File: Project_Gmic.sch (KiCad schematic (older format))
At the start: 44 parts, among them J1 SecondaryBoard_L, J2 SecondaryBoard_R, SW1 SW_SPST, U1 ADA4807-1, U2 ADA4807-4, U3 ADA4807-1, U4 XC6351A120MR-G

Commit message: butterworth filter, new aop, cleaning
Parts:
- removed C2, C5: 100pF, Capacitor_SMD:C_0805_2012Metric, symbol Device:C
- removed R11, R12, R6: 10k, Resistor_SMD:R_0805_2012Metric, symbol Device:R
- removed R4, R7: 80k, Resistor_SMD:R_0805_2012Metric, symbol Device:R
- removed SW1: SW_SPST, Button_Switch_SMD:SW_DIP_SPSTx01_Slide_9.78x4.72mm_W8.61mm_P2.54mm, symbol Switch:SW_SPST
- removed U1, U3: ADA4807-1, Package_TO_SOT_SMD:SOT-23-6_Handsoldering, symbol Amplifier_Operational:ADA4807-1
- removed U2: ADA4807-4, Package_SO:SOIC-14_3.9x8.7mm_P1.27mm, symbol Amplifier_Operational:ADA4807-4
- added C? (x3): 100pF, Capacitor_SMD:C_0805_2012Metric, symbol Device:C
- added J?: AudioJack2_Ground, symbol Connector:AudioJack2_Ground
- added J?: USB_C_Receptacle_USB2.0, symbol Connector:USB_C_Receptacle_USB2.0
- added R? (x3): 80k, Resistor_SMD:R_0805_2012Metric, symbol Device:R
- added RV?: R_Potentiometer, symbol Device:R_Potentiometer
- added SW?: SW_SPDT, symbol Switch:SW_SPDT
- added U? (x2): MCP6476U, Package_TO_SOT_SMD:SOT-23-5, symbol Custom:MCP6476U
- added U? (x5): MCP6479, symbol Custom:MCP6479
- MK1: value Microphone1 -> CMC-9745-44P
- MK2: value Microphone2 -> CMC-9745-44P
- R1, R2: value 200k -> 2.2k
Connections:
- net labels added: AUDIO_AVERAGE, AUDIO_OUT, AUDIO_PASS_HIGH, AUDIO_PASS_LOW
- net labels removed: Uout_average, Uout_highFilter, Uout_lowFilter, ~DISABLE
- wire segments 173 -> 184
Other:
- note added: "2x Audio input"
- note added: "Audio average and pre-amp"
- note added: "Low-pass Filter"
- note removed: "Audio average"
- note removed: "Audio input"
- note removed: "Filter"
- moved on the sheet: C1, C4, R10, R3, R5, R8

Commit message: Set connectors, preparing usb-c
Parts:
- removed J1: SecondaryBoard_L, Connector_PinHeader_2.54mm:PinHeader_1x03_P2.54mm_Horizontal, symbol Connector:Conn_01x03_Male
- removed J2: SecondaryBoard_R, Connector_PinHeader_2.54mm:PinHeader_1x03_P2.54mm_Horizontal, symbol Connector:Conn_01x03_Male
- added R? (x2): R, symbol Device:R
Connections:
- net labels removed: R_POT_IN, R_POT_OUT, Uout
- wire segments 184 -> 190
- no-connect marks 0 -> 6
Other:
- note removed: "SecondaryBoard"
- moved on the sheet: J?
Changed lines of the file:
@@
 Wire Wire Line
 	10200 5750 9600 5750
-$Comp
-L Connector:Conn_01x03_Male J1
-U 1 1 5EEDDD06
-P 1000 5350
-F 0 "J1" H 1108 5631 50  0000 C CNN
-F 1 "SecondaryBoard_L" H 1108 5540 50  0000 C CNN
-F 2 "Connector_PinHeader_2.54mm:PinHeader_1x03_P2.54mm_Horizontal" H 1000 5350 50  0001 C CNN
-F 3 "~" H 1000 5350 50  0001 C CNN
-	1    1000 5350
-	1    0    0    -1
-$EndComp
-$Comp
-L Connector:Conn_01x03_Male J2
-U 1 1 5EEDF161
-P 1000 6100
-F 0 "J2" H 1108 6381 50  0000 C CNN
-F 1 "SecondaryBoard_R" H 1108 6290 50  0000 C CNN
-F 2 "Connector_PinHeader_2.54mm:PinHeader_1x03_P2.54mm_Horizontal" H 1000 6100 50  0001 C CNN
-F 3 "~" H 1000 6100 50  0001 C CNN
-	1    1000 6100
-	1    0    0    -1
-$EndComp
-$Comp
-L power:+5V #PWR0134
-U 1 1 5EEDFB92
-P 1500 5150
-F 0 "#PWR0134" H 1500 5000 50  0001 C CNN
-F 1 "+5V" H 1515 5323 50  0000 C CNN
-F 2 "" H 1500 5150 50  0001 C CNN
-F 3 "" H 1500 5150 50  0001 C CNN
-	1    1500 5150
-	1    0    0    -1
-$EndComp
-Wire Wire Line
-	1200 5250 1500 5250
-Wire Wire Line
-	1500 5250 1500 5150
-$Comp
-L power:GND #PWR0135
-U 1 1 5EEEA4DA
-P 1500 6300
-F 0 "#PWR0135" H 1500 6050 50  0001 C CNN
-F 1 "GND" H 1505 6127 50  0000 C CNN
-F 2 "" H 1500 6300 50  0001 C CNN
-F 3 "" H 1500 6300 50  0001 C CNN
-	1    1500 6300
-	1    0    0    -1
-$EndComp
-Wire Wire Line
-	1500 6200 1200 6200
-Wire Wire Line
-	1500 6300 1500 6200
-Text Label 1200 6100 0    50   ~ 0
-Uout
-Text Label 1200 5350 0    50   ~ 0
-R_POT_IN
-Text Label 1200 5450 0    50   ~ 0
-R_POT_OUT
-Wire Wire Line
-	1500 6200 1500 6000
-Wire Wire Line
-	1500 6000 1200 6000
-Connection ~ 1500 6200
-Wire Notes Line
-	750  4900 1650 4900
-Wire Notes Line
-	1650 4900 1650 6500
-Wire Notes Line
-	1650 6500 750  6500
-Wire Notes Line
-	750  6500 750  4900
-Text Notes 750  4900 0    50   ~ 0
-SecondaryBoard
 Text Notes 2800 600  0    50   ~ 0
 https://www.mouser.ch/ProductDetail/CUI-Devices/CMC-9745-44P?qs=48I1WSKJTyYn9Sr%252BBph%2FcA%3D%3D
@@
 L Connector:USB_C_Receptacle_USB2.0 J?
 U 1 1 62617E06
-P 1000 9050
-F 0 "J?" H 1107 9917 50  0000 C CNN
-F 1 "USB_C_Receptacle_USB2.0" H 1107 9826 50  0000 C CNN
-F 2 "" H 1150 9050 50  0001 C CNN
-F 3 "https://www.usb.org/sites/default/files/documents/usb_type-c.zip" H 1150 9050 50  0001 C CNN
-	1    1000 9050
-	1    0    0    -1
-$EndComp
+P -1300 6100
+F 0 "J?" H -1193 6967 50  0000 C CNN
+F 1 "USB_C_Receptacle_USB2.0" H -1193 6876 50  0000 C CNN
+F 2 "" H -1150 6100 50  0001 C CNN
+F 3 "https://www.usb.org/sites/default/files/documents/usb_type-c.zip" H -1150 6100 50  0001 C CNN
+	1    -1300 6100
+	1    0    0    -1
+$EndComp
+NoConn ~ -700 6000
+NoConn ~ -700 6100
+NoConn ~ -700 6300
+NoConn ~ -700 6200
+$Comp
+L power:GND #PWR?
+U 1 1 6226F1C9
+P -1300 7100
+F 0 "#PWR?" H -1300 6850 50  0001 C CNN
+F 1 "GND" H -1295 6927 50  0000 C CNN
+F 2 "" H -1300 7100 50  0001 C CNN
+F 3 "" H -1300 7100 50  0001 C CNN
+	1    -1300 7100
+	1    0    0    -1
+$EndComp
+Wire Wire Line
+	-1300 7100 -1300 7050
+Wire Wire Line
+	-1300 7050 -1600 7050
+Wire Wire Line
+	-1600 7050 -1600 7000
+Connection ~ -1300 7050
+Wire Wire Line
+	-1300 7050 -1300 7000
+NoConn ~ -700 6600
+NoConn ~ -700 6700
+$Comp
+L Device:R R?
+U 1 1 62299238
+P -450 6200
+F 0 "R?" H -380 6246 50  0000 L CNN
+F 1 "R" H -380 6155 50  0000 L CNN
+F 2 "" V -520 6200 50  0001 C CNN
+F 3 "~" H -450 6200 50  0001 C CNN
+	1    -450 6200
+	1    0    0    -1
+$EndComp
+$Comp
+L Device:R R?
+U 1 1 622A4AA5
+P -150 6200
+F 0 "R?" H -80 6246 50  0000 L CNN
+F 1 "R" H -80 6155 50  0000 L CNN
+F 2 "" V -220 6200 50  0001 C CNN
+F 3 "~" H -150 6200 50  0001 C CNN
+	1    -150 6200
+	1    0    0    -1
+$EndComp
+Wire Wire Line
+	-450 6050 -450 5800
+Wire Wire Line
+	-450 5800 -700 5800
+Wire Wire Line
+	-700 5700 -150 5700
+Wire Wire Line
+	-150 5700 -150 6050
+Wire Wire Line
+	-450 6350 -450 7050
+Wire Wire Line
+	-450 7050 -1300 7050
+Wire Wire Line
+	-450 7050 -150 7050
+Wire Wire Line
+	-150 7050 -150 6350
+Connection ~ -450 7050
 $EndSCHEMATC

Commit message: Schematics improvement, file cleaning
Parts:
- removed C10, C12, C16, C19: 10uF, Capacitor_SMD:CP_Elec_4x4.5, symbol Device:C_Polarized
- removed C11, C9: 100nF, Capacitor_SMD:C_0805_2012Metric, symbol Device:C
- removed C18: 1uF, Capacitor_SMD:CP_Elec_4x4.5, symbol Device:C_Polarized
- added C13, C17, C19, C20, C8: 100nF, Capacitor_SMD:C_0805_2012Metric, symbol Device:C
- added D1: D_Schottky, symbol Device:D_Schottky
- added L1, L2: L, symbol Device:L
- added R13: 80k, Resistor_SMD:R_0805_2012Metric, symbol Device:R
- C1, C2: renamed from C?; value 1uF -> 2.2uF
- C10: renamed from C6; value 10uF -> 1uF
- C12: renamed from C8; value 10uF -> 1uF
- R3, R4: renamed from R?; value R -> 5.1k
- gave numbers to parts that had none: 15
- renumbered C7 to C11, C15 to C14, C13 to C15, C14 to C16, C17 to C18, C1 to C3, C4 to C5, C3 to C7, R8 to R11, R9 to R14, R10 to R15, R1 to R6, R2 to R7, R5 to R8, R3 to R9
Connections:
- net +5V: now also J1.A4 (VBUS), J1.A9 (VBUS), J1.B4 (VBUS), J1.B9 (VBUS), C13.1, C17.1
- net -5V: now also C19.2, C20.2
- net AUDIO_PASS_HIGH: now also R11.1
- net GND: now also L1.1, L2.1; no longer C10.2, C11.1, C12.1, C14.2, C18.1, C4.1, C7.2, C9.1, J2.G, J2.T, MK1.1 (-), MK2.1 (-), R11.1, R8.1, SW1.3 (C), U2.1 (+), U3.1 (+)
- net at C5.1, R11.2: now also C8.2; no longer U1.10 (+)
- net at J2.S: now also D1.1 (K); no longer SW1.2 (B)
- new net: C8.1, R13.2, U1.10 (+)
- new net: D1.2 (A), SW1.2 (B)
- new net GNDA: C10.2, C11.1, C12.1, C13.2, C14.2, C17.2, C18.1, C19.1, C20.1, C4.1, C7.2, C9.1, J2.G, J2.T, L1.2, L2.2, MK1.1 (-), MK2.1 (-), R13.1, R8.1, SW1.3 (C), U2.1 (+), U3.1 (+)
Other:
- note added: "High-pass Filter"
- note added: "This source describes Open Hardware and is licensed\nunder the CERN-OHL-W v2 or later. \n\nYou may redistribute and modify this documentation and make products\nusing it under the terms of the CERN-OHL-W v2 (https:/cern.ch/cern-ohl).\nThis documentation is distributed WITHOUT ANY EXPRESS OR IMPLIED WARRANTY,\nINCLUDING OF MERCHANTABILITY, SATISFACTORY QUALITY AND FITNESS FOR\nA PARTICULAR PURPOSE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"
- moved on the sheet: C14, C15, C16, C18, C5, J1, J2, R11, R14, R15, R3, R4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

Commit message: Searching for parts
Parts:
- removed D1: D_Schottky, symbol Device:D_Schottky
- removed J2: AudioJack2_Ground, symbol Connector:AudioJack2_Ground
- removed L1, L2: L, symbol Device:L
- added J2: SJ1-3523N, SJ13523N:SJ13523N, symbol Custom:SJ1-3523N
- added L1, L2: BLM21PG331SN1D, Inductor_SMD:L_0805_2012Metric, symbol Device:L_Ferrite
- C1, C2: footprint (none) -> Capacitor_SMD:C_0805_2012Metric
- J1: value USB_C_Receptacle_USB2.0 -> USB4085-GF-A; footprint (none) -> Connector_USB:USB_C_Receptacle_GCT_USB4085
- MK1, MK2: footprint Battery:BatteryHolder_Keystone_104_1x23mm -> CMC974544P:CMC974544P
- R1, R2, R3, R4: footprint (none) -> Resistor_SMD:R_0805_2012Metric
- RV1: value R_Potentiometer -> P160KN-0QC15C500K; footprint (none) -> Potentiometer_THT:Potentiometer_Alps_RK09K_Single_Horizontal
- SW1: footprint (none) -> Button_Switch_SMD:SW_SPDT_PCM12
- U1: footprint (none) -> Package_SO:SOIC-14_3.9x8.7mm_P1.27mm
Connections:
- net GND: now also L1.1, L2.1
- net GNDA: now also J2.1, L1.2, L2.2
- net at SW1.2 (B): now also J2.2
- no-connect marks 6 -> 9
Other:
- moved on the sheet: SW1

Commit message: First iteration of the PCB, Rpot
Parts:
- C10, C12, C15, C16: footprint Capacitor_SMD:CP_Elec_4x4.5 -> Capacitor_SMD:C_0805_2012Metric
- RV1: footprint Potentiometer_THT:Potentiometer_Alps_RK09K_Single_Horizontal -> P160KN0QC15C250K:P160KN0QC15C250K
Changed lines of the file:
@@
 F 0 "C10" H 5318 1646 50  0000 L CNN
 F 1 "1uF" H 5318 1555 50  0000 L CNN
-F 2 "Capacitor_SMD:CP_Elec_4x4.5" H 5238 1450 50  0001 C CNN
+F 2 "Capacitor_SMD:C_0805_2012Metric" H 5238 1450 50  0001 C CNN
 F 3 "~" H 5200 1600 50  0001 C CNN
 	1    5200 1600
@@
 F 0 "C12" H 6268 1646 50  0000 L CNN
 F 1 "1uF" H 6268 1555 50  0000 L CNN
-F 2 "Capacitor_SMD:CP_Elec_4x4.5" H 6188 1450 50  0001 C CNN
+F 2 "Capacitor_SMD:C_0805_2012Metric" H 6188 1450 50  0001 C CNN
 F 3 "~" H 6150 1600 50  0001 C CNN
 	1    6150 1600
@@
 F 0 "C15" H 9318 4546 50  0000 L CNN
 F 1 "1uF" H 9318 4455 50  0000 L CNN
-F 2 "Capacitor_SMD:CP_Elec_4x4.5" H 9238 4350 50  0001 C CNN
+F 2 "Capacitor_SMD:C_0805_2012Metric" H 9238 4350 50  0001 C CNN
 F 3 "~" H 9200 4500 50  0001 C CNN
 	1    9200 4500
@@
 F 0 "C16" H 9318 5046 50  0000 L CNN
 F 1 "1uF" H 9318 4955 50  0000 L CNN
-F 2 "Capacitor_SMD:CP_Elec_4x4.5" H 9238 4850 50  0001 C CNN
+F 2 "Capacitor_SMD:C_0805_2012Metric" H 9238 4850 50  0001 C CNN
 F 3 "~" H 9200 5000 50  0001 C CNN
 	1    9200 5000
@@
 F 0 "RV1" V 7700 3650 50  0000 R CNN
 F 1 "P160KN-0QC15C500K " V 7900 4500 50  0000 R CNN
-F 2 "Potentiometer_THT:Potentiometer_Alps_RK09K_Single_Horizontal" H 7800 3550 50  0001 C CNN
+F 2 "P160KN0QC15C250K:P160KN0QC15C250K" H 7800 3550 50  0001 C CNN
 F 3 "~" H 7800 3550 50  0001 C CNN
 	1    7800 3550
@@
 	9750 3100 10250 3100
 $Comp
-L power:GNDA #PWR?
+L power:GNDA #PWR0125
 U 1 1 629D4586
 P 10450 3500
-F 0 "#PWR?" H 10450 3250 50  0001 C CNN
+F 0 "#PWR0125" H 10450 3250 50  0001 C CNN
 F 1 "GNDA" H 10455 3327 50  0000 C CNN
 F 2 "" H 10450 3500 50  0001 C CNN

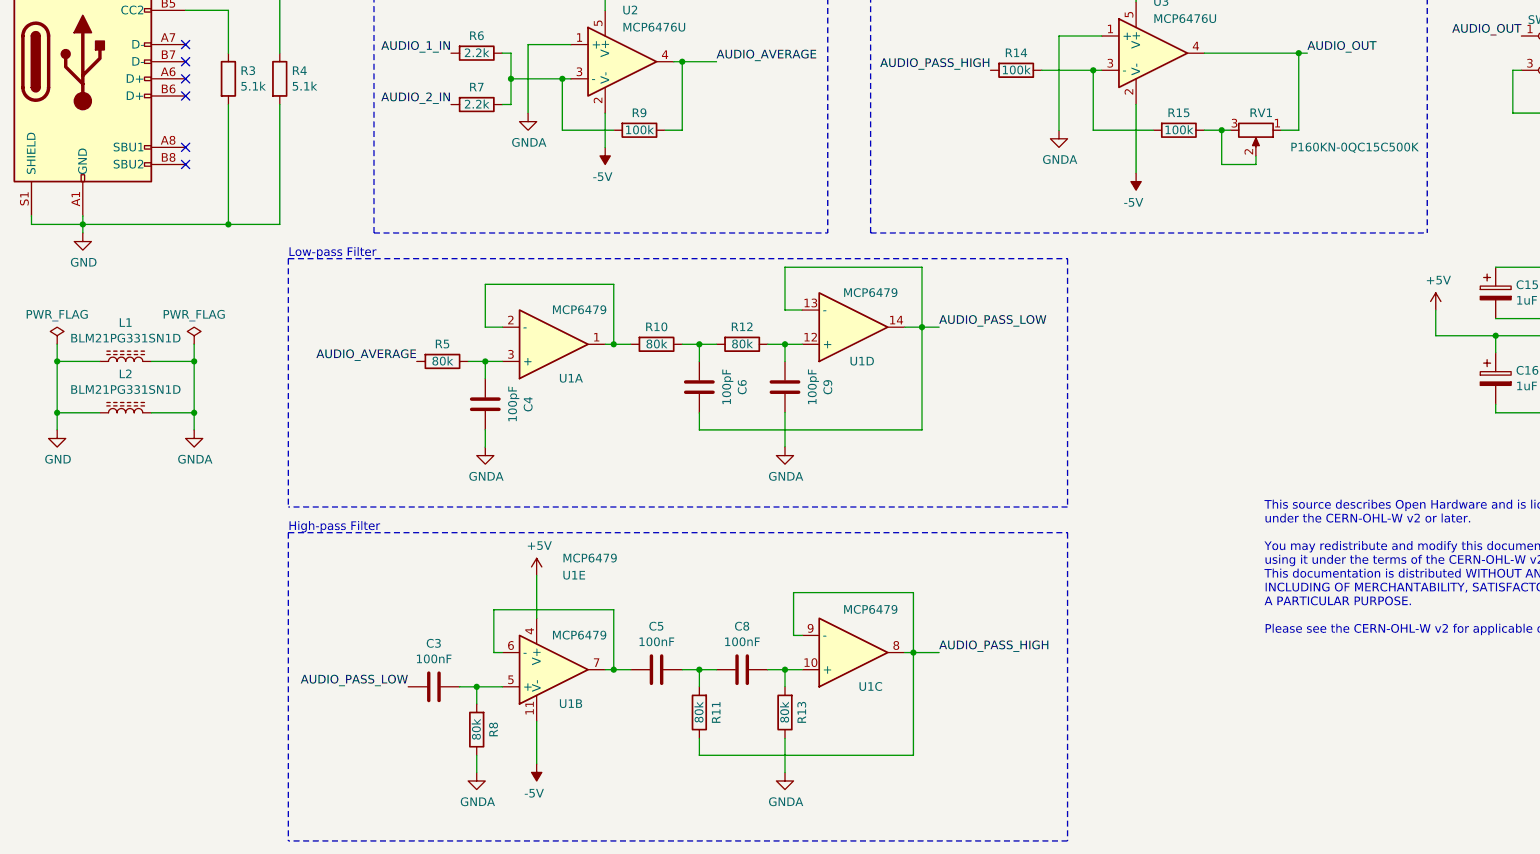
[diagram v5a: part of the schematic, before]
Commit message: Changing the potentiometer, finishing placement and board
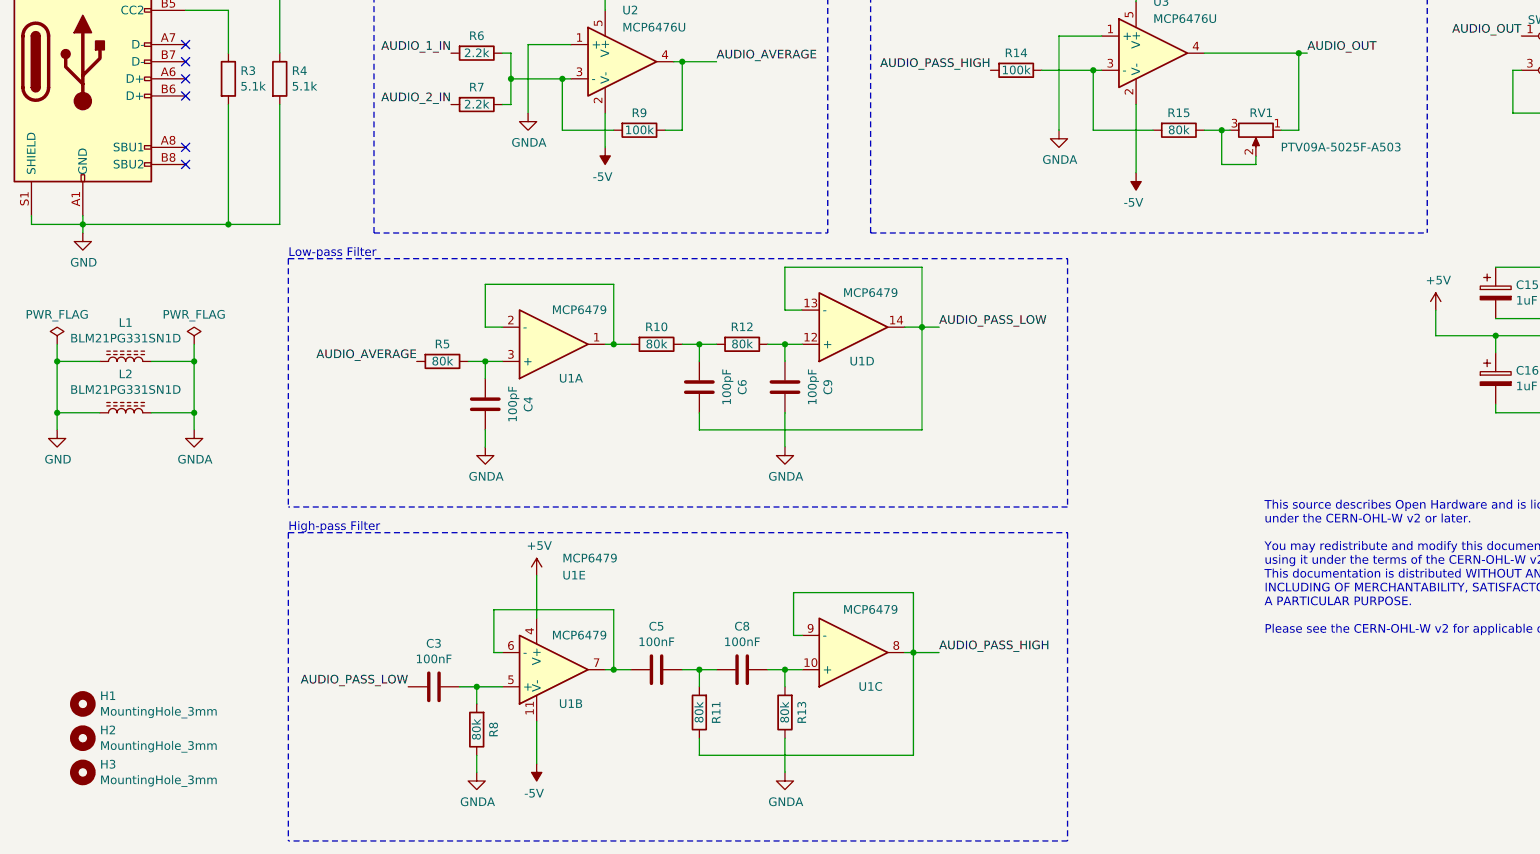
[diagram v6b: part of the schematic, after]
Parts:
- added H1, H2, H3: MountingHole_3mm, MountingHole:MountingHole_3mm, symbol Mechanical:MountingHole
- R15: value 100k -> 80k
- RV1: value P160KN-0QC15C500K -> PTV09A-5025F-A503; footprint P160KN0QC15C250K:P160KN0QC15C250K -> Potentiometer_THT:Potentiometer_Alpha_RD901F-40-00D_Single_Vertical_CircularHoles
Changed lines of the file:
@@
 P 7350 3550
 F 0 "R15" V 7250 3550 50  0000 C CNN
-F 1 "100k" V 7350 3550 50  0000 C CNN
+F 1 "80k" V 7350 3550 50  0000 C CNN
 F 2 "Resistor_SMD:R_0805_2012Metric" V 7280 3550 50  0001 C CNN
 F 3 "~" H 7350 3550 50  0001 C CNN
@@
 P 7800 3550
 F 0 "RV1" V 7700 3650 50  0000 R CNN
-F 1 "P160KN-0QC15C500K " V 7900 4500 50  0000 R CNN
-F 2 "P160KN0QC15C250K:P160KN0QC15C250K" H 7800 3550 50  0001 C CNN
+F 1 "PTV09A-5025F-A503" V 7900 4400 50  0000 R CNN
+F 2 "Potentiometer_THT:Potentiometer_Alpha_RD901F-40-00D_Single_Vertical_CircularHoles" H 7800 3550 50  0001 C CNN
 F 3 "~" H 7800 3550 50  0001 C CNN
 	1    7800 3550
@@
 	1    0    0    -1
 $EndComp
+$Comp
+L Mechanical:MountingHole H1
+U 1 1 6287E692
+P 950 6900
+F 0 "H1" H 1050 6946 50  0000 L CNN
+F 1 "MountingHole_3mm" H 1050 6855 50  0000 L CNN
+F 2 "MountingHole:MountingHole_3mm" H 950 6900 50  0001 C CNN
+F 3 "~" H 950 6900 50  0001 C CNN
+	1    950  6900
+	1    0    0    -1
+$EndComp
+$Comp
+L Mechanical:MountingHole H2
+U 1 1 6287EFDC
+P 950 7100
+F 0 "H2" H 1050 7146 50  0000 L CNN
+F 1 "MountingHole_3mm" H 1050 7055 50  0000 L CNN
+F 2 "MountingHole:MountingHole_3mm" H 950 7100 50  0001 C CNN
+F 3 "~" H 950 7100 50  0001 C CNN
+	1    950  7100
+	1    0    0    -1
+$EndComp
+$Comp
+L Mechanical:MountingHole H3
+U 1 1 6287F2F2
+P 950 7300
+F 0 "H3" H 1050 7346 50  0000 L CNN
+F 1 "MountingHole_3mm" H 1050 7255 50  0000 L CNN
+F 2 "MountingHole:MountingHole_3mm" H 950 7300 50  0001 C CNN
+F 3 "~" H 950 7300 50  0001 C CNN
+	1    950  7300
+	1    0    0    -1
+$EndComp
